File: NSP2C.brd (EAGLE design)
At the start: 58.1 x 73.7 mm, 21 parts, among them Q1 600mA/40V, Q2 IRF540

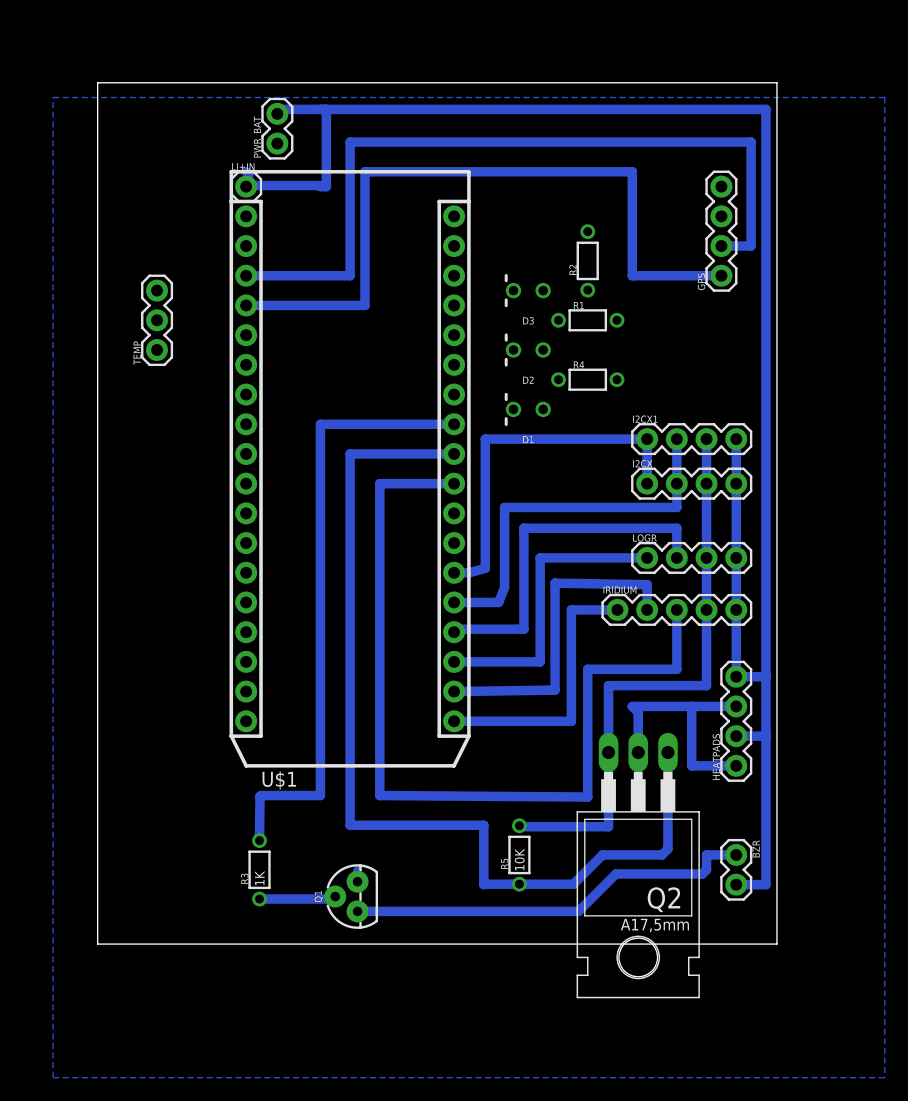
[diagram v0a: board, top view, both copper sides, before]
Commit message: Added routes to PCB in 1 Lauyer (VC)
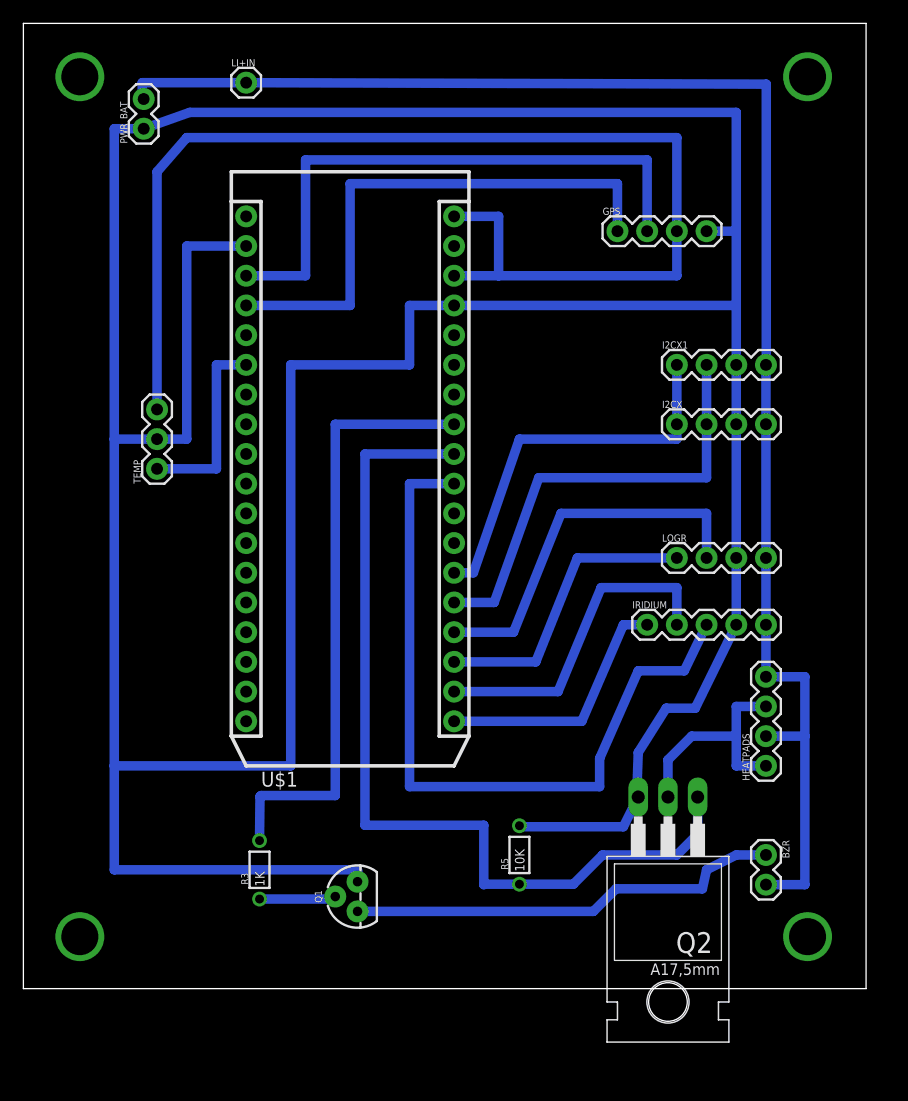
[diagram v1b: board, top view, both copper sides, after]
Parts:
- removed D1, D2, D3: (no value), SparkFun-LED:LED_3MM-NS
- removed R1, R2, R4: (no value), SparkFun-Passives:1/6W-RES
- moved PWR_BAT 11.5 mm to (0.13, 78.6)
- moved TEMP 10.2 mm to (1.27, 49.5)
- moved GPS 9.67 mm to (40.6, 69.8), turned to 0 degrees
- moved LI+IN 8.89 mm to (8.89, 82.5)
- moved I2CX1 6.84 mm to (45.7, 58.4)
- moved I2CX 5.68 mm to (45.7, 53.3)
- moved Q2 4.58 mm to (45.0, 15.1)
- moved IRIDIUM 2.84 mm to (43.2, 36.2)
- moved BZR 2.54 mm to (53.3, 16.5)
- moved HEATPADS 2.54 mm to (53.3, 24.1)
- moved LOGR 2.54 mm to (45.7, 41.9)
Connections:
- removed net N$2 (its old number): D3.K, U$1.32
- removed net N$3: D2.K, U$1.31
- removed net N$4: D1.K, U$1.30
- removed net N$5: D2.A, R1.1
- removed net N$7: D3.A, R2.1
- removed net N$8: D1.A, R4.1
- removed net VBAT: U$1.34
- net 3.3V: now also GPS.3, U$1.34; no longer GPS.4, R1.2, R2.2, R4.2
- net GND: now also GPS.4; no longer GPS.3
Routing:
- net GND: track 50.1 -> 336.8 mm
- net 3.3V: track 0.00 -> 105.9 mm
- net V_BATT: track 151.7 -> 133.5 mm
- net N$1: track 0.00 -> 16.5 mm
- net N$2: track 66.0 -> 50.3 mm
- net N$12: track 61.0 -> 46.2 mm
- net IRWKP: track 74.4 -> 64.9 mm
- net SDA: track 32.6 -> 38.8 mm
- net D3: track 82.4 -> 77.9 mm
- net N$11: track 23.2 -> 20.1 mm
- net UART4_TX: track 30.3 -> 32.6 mm
- net N$9: track 35.1 -> 37.3 mm
- net N$15: track 31.4 -> 33.6 mm
- net UART5_RX: track 23.5 -> 21.9 mm
- removed copper zone on layer 16, net N$16
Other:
- board size 58.1 x 73.7 mm -> 72.1 x 82.5 mm
